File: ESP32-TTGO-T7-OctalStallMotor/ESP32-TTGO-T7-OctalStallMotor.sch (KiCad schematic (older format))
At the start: 1 part, among them U0 TTGO-T7-v13

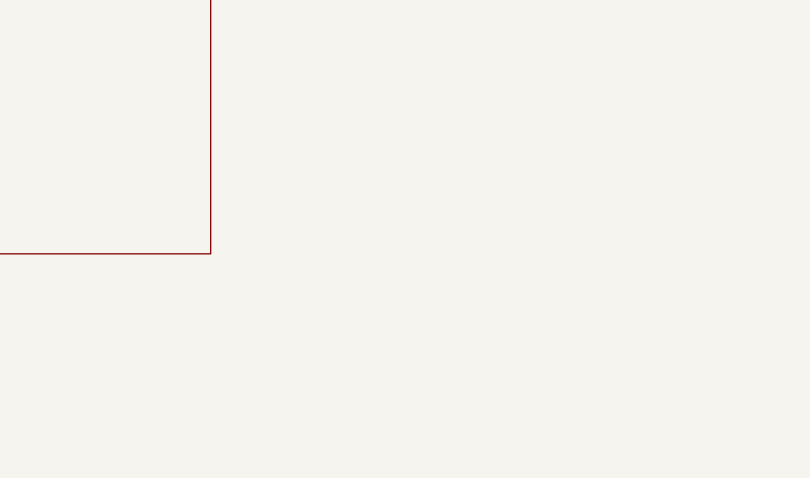
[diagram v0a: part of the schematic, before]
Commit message: Complete ESP32-TTGO-T7-OctalStallMotor PCB, start breadboard.
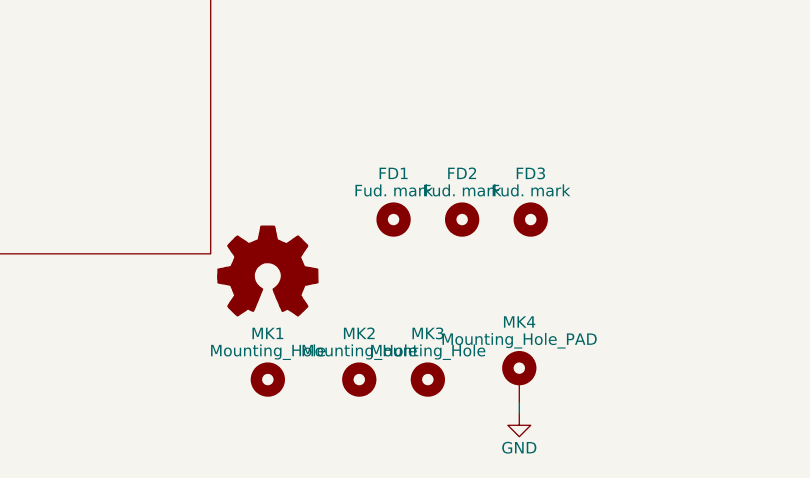
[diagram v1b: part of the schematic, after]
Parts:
- added FD1, FD2, FD3: Fud. mark, Fiducials:Fiducial_Modern_CopperTop, symbol Mounting_Hole
- added MK1, MK2, MK3: Mounting_Hole, Mounting_Holes:MountingHole_3.2mm_M3, symbol Mounting_Hole
- added MK4: Mounting_Hole_PAD, Mounting_Holes:MountingHole_3.2mm_M3_Pad_Via, symbol Mounting_Hole_PAD
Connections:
- net GND: now also MK4.1
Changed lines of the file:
@@
 LIBS:tc442x
 LIBS:4814p-2
+LIBS:mechanical
+LIBS:references
+LIBS:graphic_symbols
 LIBS:ESP32-TTGO-T7-OctalStallMotor-cache
 EELAYER 25 0
@@
 NoConn ~ 2700 2450
 $Comp
-L GND #PWR01
+L GND #PWR3
 U 1 1 621A45D6
 P 2900 3350
-F 0 "#PWR01" H 2900 3100 50  0001 C CNN
+F 0 "#PWR3" H 2900 3100 50  0001 C CNN
 F 1 "GND" H 2900 3200 50  0000 C CNN
 F 2 "" H 2900 3350 50  0001 C CNN
@@
 Connection ~ 2800 3350
 $Comp
-L +3V3 #PWR02
+L +3V3 #PWR1
 U 1 1 621A4618
 P 2800 3550
-F 0 "#PWR02" H 2800 3400 50  0001 C CNN
+F 0 "#PWR1" H 2800 3400 50  0001 C CNN
 F 1 "+3V3" H 2800 3690 50  0000 C CNN
 F 2 "" H 2800 3550 50  0001 C CNN
@@
 	2800 3550 2700 3550
 $Comp
-L +5V #PWR03
+L +5V #PWR2
 U 1 1 621A463E
 P 2800 3650
-F 0 "#PWR03" H 2800 3500 50  0001 C CNN
+F 0 "#PWR2" H 2800 3500 50  0001 C CNN
 F 1 "+5V" H 2800 3790 50  0000 C CNN
 F 2 "" H 2800 3650 50  0001 C CNN
@@
 Wire Wire Line
 	2800 3450 2700 3450
+$Comp
+L Mounting_Hole MK1
+U 1 1 6221071F
+P 5150 7500
+F 0 "MK1" H 5150 7700 50  0000 C CNN
+F 1 "Mounting_Hole" H 5150 7625 50  0000 C CNN
+F 2 "Mounting_Holes:MountingHole_3.2mm_M3" H 5150 7500 50  0001 C CNN
+F 3 "" H 5150 7500 50  0001 C CNN
+	1    5150 7500
+	1    0    0    -1
+$EndComp
+$Comp
+L Mounting_Hole MK2
+U 1 1 62210890
+P 5550 7500
+F 0 "MK2" H 5550 7700 50  0000 C CNN
+F 1 "Mounting_Hole" H 5550 7625 50  0000 C CNN
+F 2 "Mounting_Holes:MountingHole_3.2mm_M3" H 5550 7500 50  0001 C CNN
+F 3 "" H 5550 7500 50  0001 C CNN
+	1    5550 7500
+	1    0    0    -1
+$EndComp
+$Comp
+L Mounting_Hole MK3
+U 1 1 62210917
+P 5850 7500
+F 0 "MK3" H 5850 7700 50  0000 C CNN
+F 1 "Mounting_Hole" H 5850 7625 50  0000 C CNN
+F 2 "Mounting_Holes:MountingHole_3.2mm_M3" H 5850 7500 50  0001 C CNN
+F 3 "" H 5850 7500 50  0001 C CNN
+	1    5850 7500
+	1    0    0    -1
+$EndComp
+$Comp
+L Mounting_Hole_PAD MK4
+U 1 1 622109A0
+P 6250 7500
+F 0 "MK4" H 6250 7750 50  0000 C CNN
+F 1 "Mounting_Hole_PAD" H 6250 7675 50  0000 C CNN
+F 2 "Mounting_Holes:MountingHole_3.2mm_M3_Pad_Via" H 6250 7500 50  0001 C CNN
+F 3 "" H 6250 7500 50  0001 C CNN
+	1    6250 7500
+	1    0    0    -1
+$EndComp
+$Comp
+L GND #PWR4
+U 1 1 62210C0C
+P 6250 7650
+F 0 "#PWR4" H 6250 7400 50  0001 C CNN
+F 1 "GND" H 6250 7500 50  0000 C CNN
+F 2 "" H 6250 7650 50  0001 C CNN
+F 3 "" H 6250 7650 50  0001 C CNN
+	1    6250 7650
+	1    0    0    -1
+$EndComp
+Wire Wire Line
+	6250 7600 6250 7650
+$Comp
+L Logo_Open_Hardware_Small #LOGO1
+U 1 1 6221105E
+P 5150 7050
+F 0 "#LOGO1" H 5150 7325 50  0001 C CNN
+F 1 "Logo_Open_Hardware_Small" H 5150 6825 50  0001 C CNN
+F 2 "Symbols:OSHW-Logo2_14.6x12mm_SilkScreen" H 5150 7050 50  0001 C CNN
+F 3 "" H 5150 7050 50  0001 C CNN
+	1    5150 7050
+	1    0    0    -1
+$EndComp
+$Comp
+L Mounting_Hole FD1
+U 1 1 6221145D
+P 5700 6800
+F 0 "FD1" H 5700 7000 50  0000 C CNN
+F 1 "Fud. mark" H 5700 6925 50  0000 C CNN
+F 2 "Fiducials:Fiducial_Modern_CopperTop" H 5700 6800 50  0001 C CNN
+F 3 "" H 5700 6800 50  0001 C CNN
+	1    5700 6800
+	1    0    0    -1
+$EndComp
+$Comp
+L Mounting_Hole FD2
+U 1 1 62211584
+P 6000 6800
+F 0 "FD2" H 6000 7000 50  0000 C CNN
+F 1 "Fud. mark" H 6000 6925 50  0000 C CNN
+F 2 "Fiducials:Fiducial_Modern_CopperTop" H 6000 6800 50  0001 C CNN
+F 3 "" H 6000 6800 50  0001 C CNN
+	1    6000 6800
+	1    0    0    -1
+$EndComp
+$Comp
+L Mounting_Hole FD3
+U 1 1 6221166C
+P 6300 6800
+F 0 "FD3" H 6300 7000 50  0000 C CNN
+F 1 "Fud. mark" H 6300 6925 50  0000 C CNN
+F 2 "Fiducials:Fiducial_Modern_CopperTop" H 6300 6800 50  0001 C CNN
+F 3 "" H 6300 6800 50  0001 C CNN
+	1    6300 6800
+	1    0    0    -1
+$EndComp
 $EndSCHEMATC
